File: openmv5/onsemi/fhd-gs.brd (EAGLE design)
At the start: 35.6 x 16.5 mm, 54 parts, among them IC1 AR0135CS2C00SUEA0, IC2 TLV62568PDDCR, IC3 MIC5365-2.8YC5-TR, J1 DF12-36-DP, Q1 PMXB120EPEZ

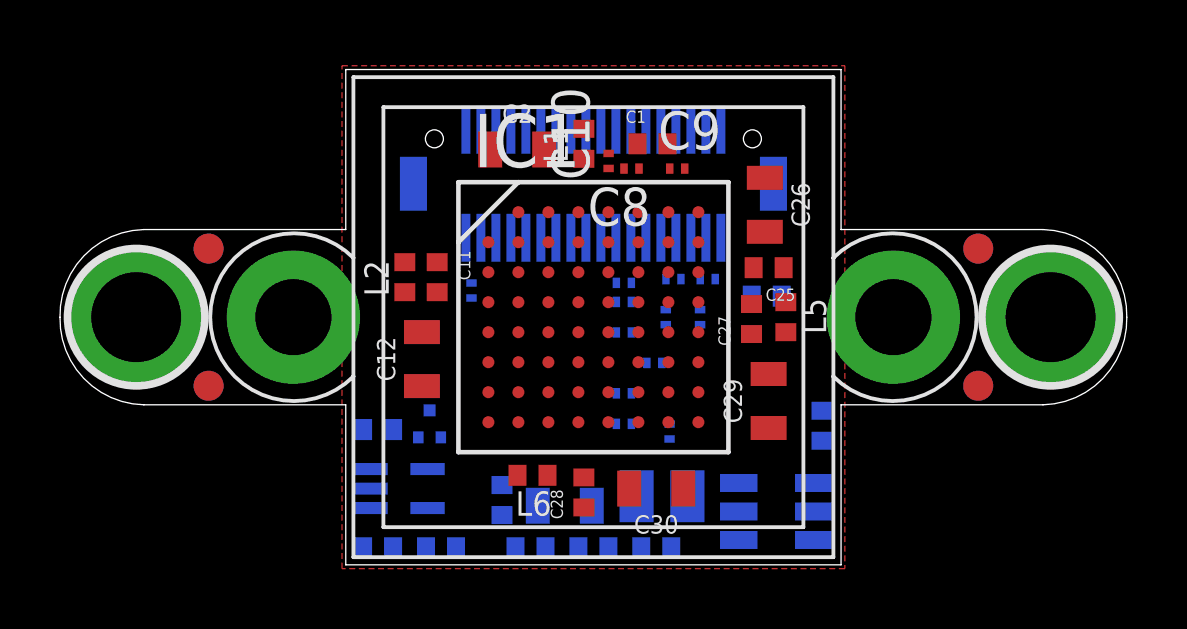
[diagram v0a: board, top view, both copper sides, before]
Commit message: Finish out new onsemi cameras
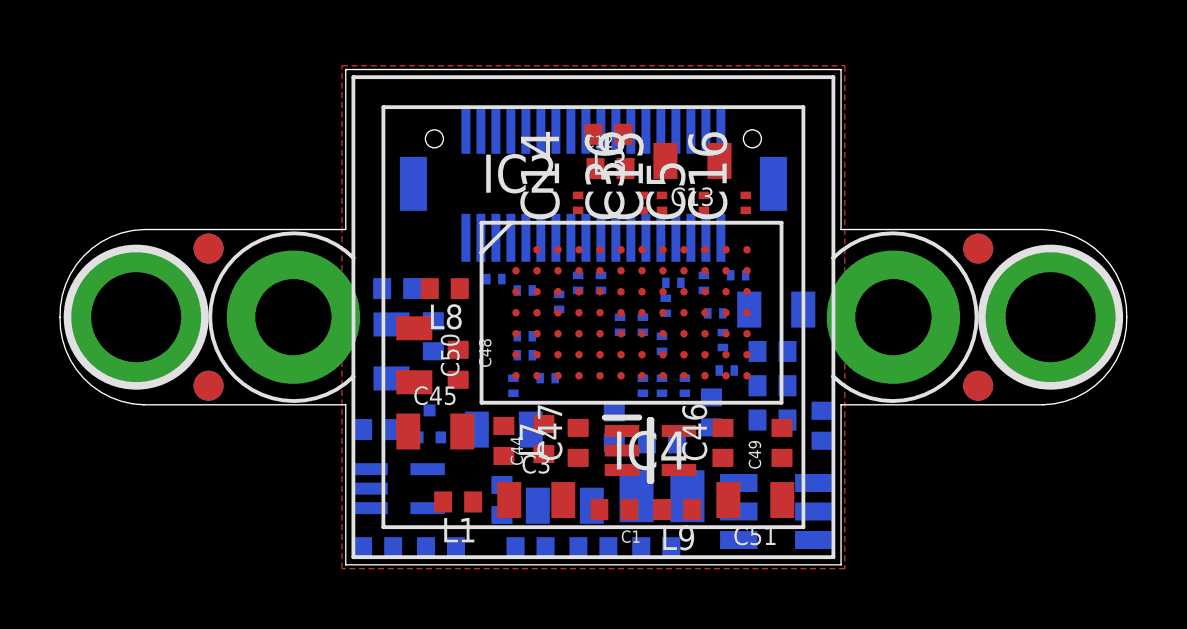
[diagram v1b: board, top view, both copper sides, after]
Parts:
- added C31, C32, C33, C34, C35, C36, C37, C38: 0.22uF, rcl:C0201
- added C39, C41, C42, C43, C44, C46, C47, C48, C49: 4.7uF, 0402:0402
- added C40, C45, C50, C51: 22uF, SparkFun-Capacitors:0805
- added IC4: MIC5365-2.8YC5-TR, MIC5365-2.8YC5-TR:SOT65P210X110-5N
- added L7, L8, L9: 100, 0402:0402
- added R5: 100K, rcl:R0402
- C11, C21, C27, C28: value 4.7uF -> 0.22uF; device 0402:0402 -> rcl:C0201
- C12, C2: value 22uF -> 4.7uF; device SparkFun-Capacitors:0805 -> 0402:0402
- C13, C3, C4: value 0.22uF -> 22uF; device rcl:C0201 -> SparkFun-Capacitors:0805
- C18: value 6.8pF -> 0.22uF; device 0402:0402 -> rcl:C0201
- C20: value 0.22uF -> 6.8pF; device rcl:C0201 -> 0402:0402
- C22, C29, C30: value 22uF -> 0.22uF; device SparkFun-Capacitors:0805 -> rcl:C0201
- C24: value 4.7uF -> 22uF; device 0402:0402 -> SparkFun-Capacitors:0805
- IC1: value AR0135CS2C00SUEA0 -> TLV62568PDDCR; device AR0135CS2C00SUEA0:AR0135CS2C00SUEA0 -> TLV62568PDDCR:SOT95P280X110-6N
- IC2: value TLV62568PDDCR -> AR0234CSSC00SUKA0; device TLV62568PDDCR:SOT95P280X110-6N -> AR0234CSSC00SUKA0:AR0234CSSC00SUKA0
- L3: value MAKK2016T2R2M -> 100; device MAKK2016T2R2M:INDC2016X100N -> 0402:0402
- L5: value 100 -> MAKK2016T2R2M; device 0402:0402 -> MAKK2016T2R2M:INDC2016X100N
- R1: value 200K -> 100K
- R4: value 100K -> 1.5K
- moved C26 13.4 mm to (11.0, 7.11), flipped to the bottom, turned to 90 degrees
- moved C23 13.3 mm to (25.4, 4.64), turned to 270 degrees
- moved L2 13.1 mm to (23.7, 4.83), flipped to the bottom, turned to 180 degrees
- moved L1 12.7 mm to (13.3, 2.10), turned to 180 degrees
- moved L4 12.3 mm to (11.2, 9.21)
- moved C1 12.3 mm to (18.5, 1.84), turned to 180 degrees
- moved L3 12.2 mm to (18.3, 14.4), flipped to the top
- moved C25 11.4 mm to (12.4, 7.62), flipped to the bottom, turned to 90 degrees
- moved R4 11.1 mm to (21.7, 5.08), turned to 90 degrees
- moved C2 10.8 mm to (23.7, 7.11), flipped to the bottom
- moved C11 9.35 mm to (21.8, 8.38), flipped to the bottom, turned to 180 degrees
- moved C12 8.94 mm to (18.4, 13.2), turned to 0 degrees
- moved IC1 8.89 mm to (23.9, 1.78), flipped to the bottom, turned to 180 degrees
- moved C29 8.52 mm to (15.1, 5.97), flipped to the bottom, turned to 270 degrees
- moved IC2 8.20 mm to (19.1, 8.40), flipped to the top, turned to 0 degrees
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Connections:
- removed net DCMI_D10: IC1.P$42, J1.24
- removed net DCMI_D11: IC1.P$43, J1.22
- removed net VDD_PLL: C11.2, C12.2, C3.1, IC1.P$8, L2.1
- new net CAP: C41.2, IC2.P$71
- new net RSVD: IC2.P$69, R4.2
- new net VAA_PHY: C39.2, C40.2, C9.1, IC2.P$67, L6.1
- new net VDDIO_PHY: C11.1, C25.2, C26.2, IC2.P$45, L4.1
- new net VDDIO_PHY_REG: C46.2, IC1.1, IC4.5, L4.2
- new net VDD_DATA: C2.2, C22.1, C4.2, IC2.P$70, L2.1
- new net VDD_PHY: C10.1, C12.2, C13.2, IC2.P$31, L3.1
- net DCMI_CLK: now also IC2.P$82; no longer IC1.P$16
- net DCMI_D0: now also IC2.P$62, J1.9; no longer IC1.P$56, J1.3
- net DCMI_D1: now also IC2.P$75, J1.7; no longer IC1.P$57, J1.1
- net DCMI_D2: now also IC2.P$76, J1.31; no longer IC1.P$58, J1.9
- net DCMI_D3: now also IC2.P$50, J1.29; no longer IC1.P$59, J1.7
- net DCMI_D4: now also IC2.P$36, J1.35; no longer IC1.P$48, J1.31
- net DCMI_D5: now also IC2.P$37, J1.28; no longer IC1.P$49, J1.29
- net DCMI_D6: now also IC2.P$14, J1.26; no longer IC1.P$50, J1.35
- net DCMI_D7: now also IC2.P$51, J1.33; no longer IC1.P$51, J1.28
- net DCMI_D8: now also IC2.P$39, J1.24; no longer IC1.P$40, J1.26
- net DCMI_D9: now also IC2.P$27, J1.22; no longer IC1.P$41, J1.33
- net DCMI_FSIN: now also IC2.P$40; no longer IC1.P$54
- net DCMI_HSYNC: now also IC2.P$30; no longer IC1.P$32
- net DCMI_PCLK: now also IC2.P$29; no longer IC1.P$34
- net DCMI_PWDN_INT: now also R5.1; no longer R4.1
- net DCMI_SCL: now also IC2.P$65; no longer IC1.P$25
- net DCMI_SDA: now also IC2.P$53; no longer IC1.P$26
- net DCMI_VSYNC: now also IC2.P$18; no longer IC1.P$33
- net FB: now also C20.2, IC1.6; no longer C18.2, IC2.6
- net GND: now also C11.2, C13.1, C18.2, C21.2, C22.2, C27.2, C28.2, C29.2, C3.1, C30.2, C31.2, C32.2, C33.2, C34.2, C35.2, C36.2, C37.2, C38.2, C39.1, C4.1, C40.1, C41.1, C42.1, C43.1, C44.1, C45.1, C46.1, C47.1, C48.1, C49.1, C50.1, C51.1, IC1.2, IC2.P$1, IC2.P$13, IC2.P$17, IC2.P$2, IC2.P$23, IC2.P$24, IC2.P$26, IC2.P$28, IC2.P$4, IC2.P$43, IC2.P$44, IC2.P$49, IC2.P$5, IC2.P$54, IC2.P$55, IC2.P$61, IC2.P$64, IC2.P$68, IC2.P$74, IC2.P$77, IC2.P$8, IC2.P$81, IC4.2, J1.1, J1.3, R4.1, R5.2; no longer C11.1, C13.2, C20.2, C21.1, C22.1, C27.1, C28.1, C29.1, C3.2, C30.1, C4.2, IC1.P$20, IC1.P$22, IC1.P$23, IC1.P$24, IC1.P$27, IC1.P$28, IC1.P$36, IC1.P$44, IC1.P$46, IC1.P$52, IC1.P$55, IC1.P$60, IC1.P$7, IC2.2, R4.2
- net RESET_N: now also IC1.5, IC2.P$66; no longer IC1.P$63, IC2.5
- net SPI_MISO: now also IC2.P$52; no longer IC1.P$35
- net SW: now also IC1.3, L5.2; no longer IC2.3, L3.2
- net VAA: now also C44.2, C45.2, C6.1, C7.1, C8.1, IC2.P$12, IC2.P$73, IC2.P$78, IC2.P$9, L7.1; no longer C25.2, C26.2, C4.1, IC1.P$14, IC1.P$15, L4.1
- net VAA_PIX: now also C27.1, C28.1, C29.1, C30.1, C48.2, C50.2, IC2.P$19, IC2.P$25, IC2.P$72, IC2.P$80, L8.1; no longer C13.1, C14.1, C27.2, C29.2, IC1.P$30, IC1.P$31, L5.1
- net VCC: now also C23.2, IC1.4; no longer C21.2, IC2.4
- net VDD: now also C14.1, C15.1, C16.1, C17.1, C18.1, C19.1, C21.1, C3.2, IC2.P$11, IC2.P$21, IC2.P$3, IC2.P$42, IC2.P$48, IC2.P$7, IC2.P$79; no longer C10.1, C2.2, C6.1, C7.1, C8.1, C9.1, IC1.P$13, IC1.P$21, IC1.P$29, IC1.P$5, IC1.P$6
- net VDDA: now also C43.2, C47.2, IC4.1; no longer C24.2
- net VDDIO: now also C31.1, C32.1, C33.1, C34.1, C35.1, C36.1, C37.1, C38.1, C49.2, C51.2, IC2.P$15, IC2.P$16, IC2.P$22, IC2.P$38, IC2.P$41, IC2.P$6, IC2.P$60, IC2.P$83, L9.1; no longer C15.1, C16.1, C17.1, C19.1, C20.1, C28.2, C30.2, IC1.P$37, IC1.P$45, IC1.P$53, IC1.P$61, IC1.P$62, L6.1
- net VDDIO_REG: now also C42.2, IC4.3, L7.2, L8.2, L9.2; no longer C23.2, IC2.1, L2.2, L4.2, L5.2
- net VDD_REG: now also C20.1, C24.2, L2.2, L3.2, L5.1; no longer C18.1, C22.2, L3.1
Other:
- board text added: "AR0234 R1"
- board text removed: "AR0135 R1"

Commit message: Update camera modules to use different non-flippable pmosfet
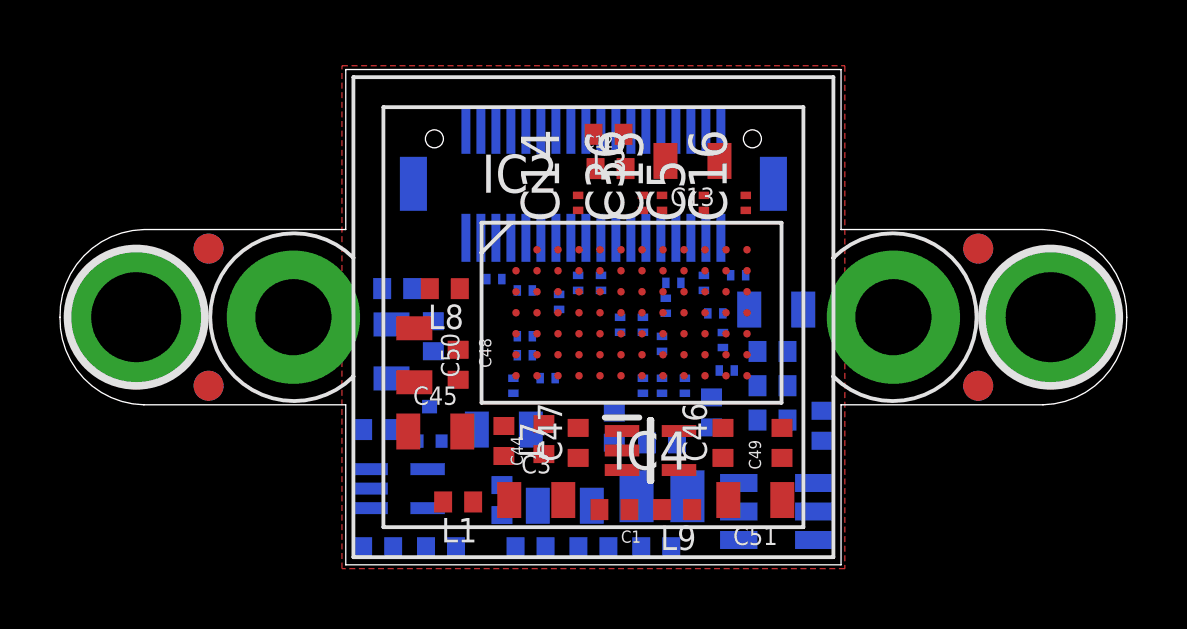
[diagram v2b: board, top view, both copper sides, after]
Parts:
- Q1: value PMXB120EPEZ -> SSM3J15FV,L3F; device PMXB120EPEZ:PMXB120EPEZ -> SSM3J15FV_L3F:SSM3J15FVL3F
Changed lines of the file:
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@@
 <attribute name="VALUE" x="15.875" y="1.27" size="0.6096" layer="27" font="vector" ratio="20" align="top-center"/>
 </element>
-<element name="Q1" library="PMXB120EPEZ" package="PMXB120EPEZ" value="PMXB120EPEZ" x="12.319" y="4.699" smashed="yes" rot="MR0">
-<attribute name="DESCRIPTION" value="MOSFET 30 V, P-channel Trench MOSFET" x="15.367" y="4.699" size="1.778" layer="28" rot="MR0" display="off"/>
-<attribute name="HEIGHT" value="0.4mm" x="15.367" y="4.699" size="1.778" layer="28" rot="MR0" display="off"/>
-<attribute name="MANUFACTURER_NAME" value="Nexperia" x="15.367" y="4.699" size="1.778" layer="28" rot="MR0" display="off"/>
-<attribute name="MANUFACTURER_PART_NUMBER" value="PMXB120EPEZ" x="15.367" y="4.699" size="1.778" layer="28" rot="MR0" display="off"/>
-<attribute name="MOUSER_PART_NUMBER" value="771-PMXB120EPEZ" x="15.367" y="4.699" size="1.778" layer="28" rot="MR0" display="off"/>
-<attribute name="MOUSER_PRICE-STOCK" value="https://www.mouser.co.uk/ProductDetail/Nexperia/PMXB120EPEZ?qs=gNSudQoqUYCYLaOobF3dPA%3D%3D" x="15.367" y="4.699" size="1.778" layer="28" rot="MR0" display="off"/>
-<attribute name="MPN" value="PMXB120EPEZ" x="15.367" y="4.699" size="1.778" layer="28" rot="MR0" display="off"/>
+<element name="Q1" library="SSM3J15FV_L3F" package="SSM3J15FVL3F" value="SSM3J15FV,L3F" x="12.319" y="4.699" smashed="yes" rot="MR0">
+<attribute name="DESCRIPTION" value="MOSFET Small-signal MOSFET High Speed Switching" x="15.367" y="4.699" size="1.778" layer="28" rot="MR0" display="off"/>
+<attribute name="HEIGHT" value="0.55mm" x="15.367" y="4.699" size="1.778" layer="28" rot="MR0" display="off"/>
+<attribute name="MANUFACTURER_NAME" value="Toshiba" x="15.367" y="4.699" size="1.778" layer="28" rot="MR0" display="off"/>
+<attribute name="MANUFACTURER_PART_NUMBER" value="SSM3J15FV,L3F" x="15.367" y="4.699" size="1.778" layer="28" rot="MR0" display="off"/>
+<attribute name="MOUSER_PART_NUMBER" value="757-SSM3J15FVL3F" x="15.367" y="4.699" size="1.778" layer="28" rot="MR0" display="off"/>
+<attribute name="MOUSER_PRICE-STOCK" value="https://www.mouser.co.uk/ProductDetail/Toshiba/SSM3J15FVL3F?qs=PDgMCp4xDJb4qTgE7FAUzA%3D%3D" x="15.367" y="4.699" size="1.778" layer="28" rot="MR0" display="off"/>
+<attribute name="MPN" value="SSM3J15FV,L3F" x="15.367" y="4.699" size="1.778" layer="28" rot="MR0" display="off"/>
 <attribute name="NAME" x="12.319" y="4.699" size="1.27" layer="26" rot="MR0" align="center"/>
 <attribute name="VALUE" x="12.319" y="4.699" size="1.27" layer="28" rot="MR0" align="center"/>
@@
 <contactref element="IC4" pad="1"/>
 <contactref element="C47" pad="2"/>
-<wire x1="18.735" y1="4.46" x2="17.272" y2="4.564" width="0" layer="19" extent="1-1"/>
-<wire x1="10.1045" y1="0.5715" x2="17.272" y2="4.564" width="0" layer="19" extent="1-16"/>
-<wire x1="10.353" y1="1.89" x2="10.1045" y2="0.5715" width="0" layer="19" extent="16-16"/>
-<wire x1="11.944" y1="4.249" x2="10.353" y2="1.89" width="0" layer="19" extent="16-16"/>
-<wire x1="21.53" y1="14.5001" x2="11.944" y2="4.249" width="0" layer="19" extent="16-16"/>
+<wire x1="18.735" y1="4.46" x2="21.53" y2="14.5001" width="0" layer="19" extent="1-16"/>
+<wire x1="17.272" y1="4.564" x2="18.735" y2="4.46" width="0" layer="19" extent="1-1"/>
+<wire x1="11.919" y1="4.124" x2="17.272" y2="4.564" width="0" layer="19" extent="1-16"/>
+<wire x1="10.353" y1="1.89" x2="11.919" y2="4.124" width="0" layer="19" extent="16-16"/>
+<wire x1="10.1045" y1="0.5715" x2="10.353" y2="1.89" width="0" layer="19" extent="16-16"/>
 </signal>
 <signal name="VCC" class="3">
@@
 <contactref element="J1" pad="25"/>
 <contactref element="Q1" pad="1"/>
-<wire x1="16.03" y1="10.8999" x2="12.694" y2="4.249" width="0" layer="19" extent="1-16"/>
+<wire x1="12.719" y1="4.124" x2="16.03" y2="10.8999" width="0" layer="19" extent="16-16"/>
 </signal>
 <signal name="DCMI_D2" class="4">
@@
 <contactref element="R5" pad="1"/>
 <contactref element="Q1" pad="3"/>
-<wire x1="11.1045" y1="4.5085" x2="10.353" y2="3.19" width="0" layer="19" extent="16-16"/>
-<wire x1="12.319" y1="5.149" x2="11.1045" y2="4.5085" width="0" layer="19" extent="16-16"/>
+<wire x1="11.1045" y1="4.5085" x2="12.319" y2="5.274" width="0" layer="19" extent="16-16"/>
+<wire x1="10.353" y1="3.19" x2="11.1045" y2="4.5085" width="0" layer="19" extent="16-16"/>
 </signal>
 <signal name="RESET_N" class="4">
